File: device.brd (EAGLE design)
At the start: 38 x 50 mm, 40 parts, among them CON1 B3B-ZR, CON2 B3B-ZR, CON3 B3B-ZR, CON4 B3B-ZR, CON5 B3B-ZR, J1 S2B-PH-SM4-TB(LF)(SN), Q1 2SC2712-GR(F), Q2 2SC2712-GR(F), Q3 2SC2712-GR(F), Q4 2SC2712-GR(F)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

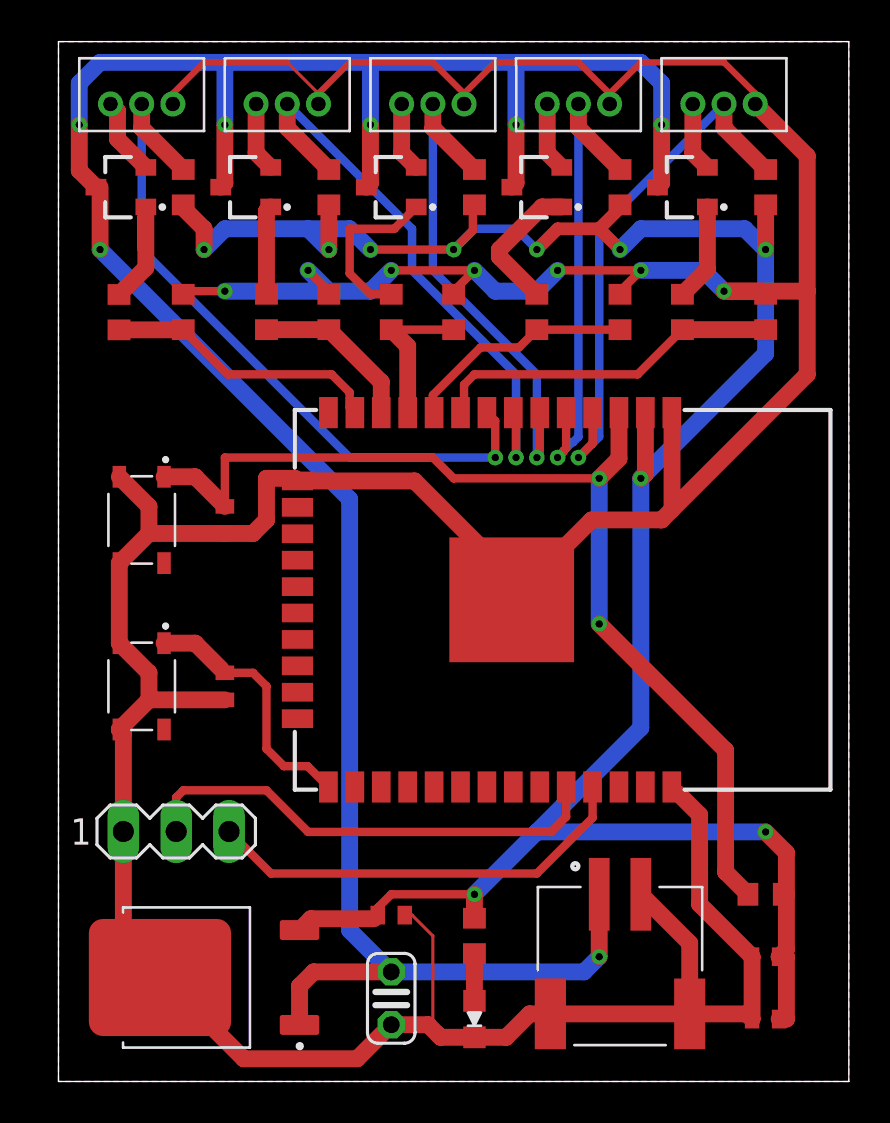
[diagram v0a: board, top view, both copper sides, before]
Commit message: Manual routing of V2.0.0
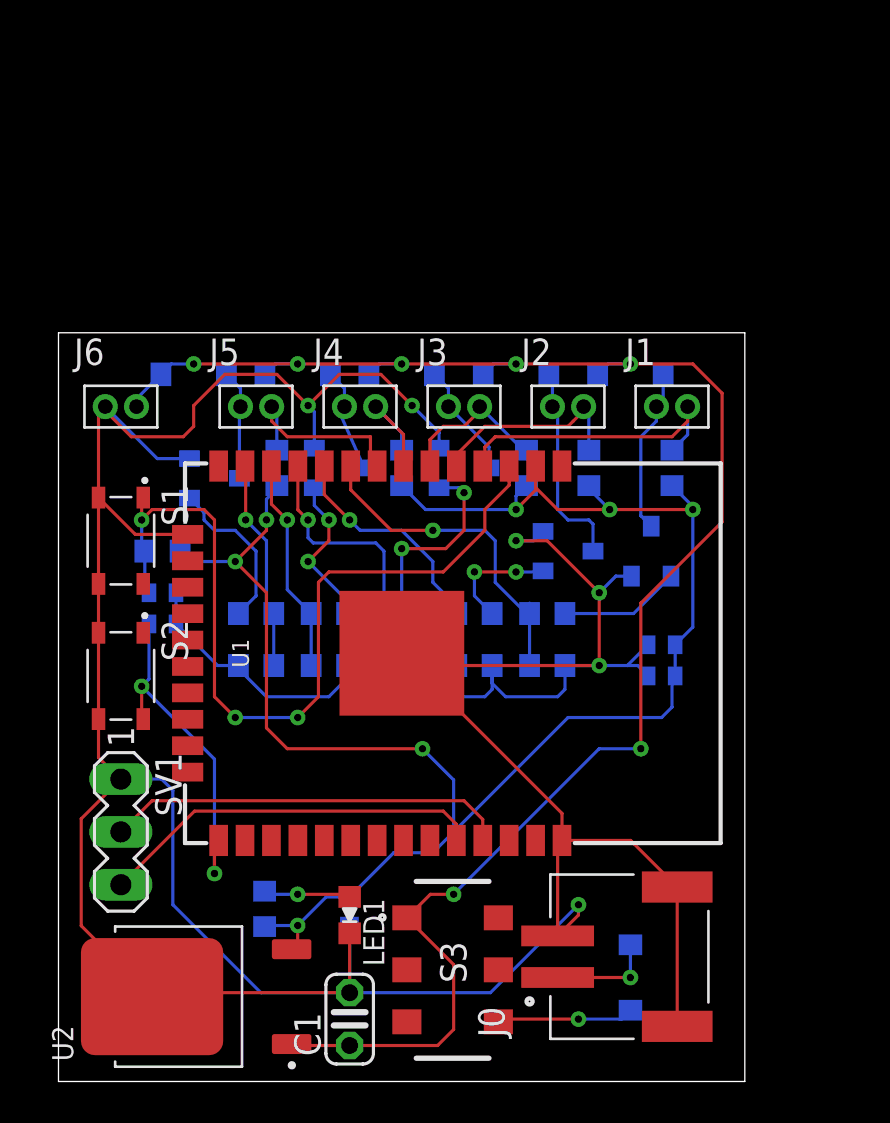
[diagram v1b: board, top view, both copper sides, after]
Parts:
- removed CON1, CON2, CON3, CON4, CON5: B3B-ZR, jst:B3B-ZR
- added D1, D2, D3, D4, D5, D6: GS1010FL, GS1010FL:SODFL3618X110N
- added J0: S2B-PH-SM4-TB(LF)(SN), S2B-PH-SM4-TB_LF__SN_:JST_S2B-PH-SM4-TB(LF)(SN)
- added J2, J3, J4, J5, J6: JST_ZH_2PIN, kanflo:JST_ZH_2PIN
- added S3: SSSS213202, SSSS213202:SSSS213202
- J1: value S2B-PH-SM4-TB(LF)(SN) -> JST_ZH_2PIN; device S2B-PH-SM4-TB_LF__SN_:JST_S2B-PH-SM4-TB(LF)(SN) -> kanflo:JST_ZH_2PIN
- moved R16 33.4 mm to (5.00, 25.5), flipped to the bottom, turned to 180 degrees
- moved J1 23.1 mm to (29.5, 32.0)
- moved R9 20.0 mm to (23.5, 20.0), flipped to the bottom, turned to 0 degrees
- moved R3 18.4 mm to (20.0, 20.0), flipped to the bottom, turned to 0 degrees
- moved Q1 17.6 mm to (28.5, 25.5), flipped to the bottom, turned to 0 degrees
- moved Q2 17.6 mm to (24.5, 25.5), flipped to the bottom
- moved R13 17.4 mm to (9.50, 20.0), flipped to the bottom, turned to 180 degrees
- moved C4 17.2 mm to (29.0, 19.5), flipped to the bottom, turned to 0 degrees
- moved R11 17.2 mm to (16.5, 20.0), flipped to the bottom, turned to 0 degrees
- moved R15 17.0 mm to (13.0, 20.0), flipped to the bottom, turned to 0 degrees
- moved R12 15.9 mm to (9.50, 22.5), flipped to the bottom, turned to 180 degrees
- moved R8 15.9 mm to (23.5, 22.5), flipped to the bottom, turned to 0 degrees
- moved C3 15.8 mm to (29.0, 21.0), flipped to the bottom, turned to 0 degrees
- moved R14 14.8 mm to (13.0, 22.5), flipped to the bottom, turned to 0 degrees
- moved R2 14.8 mm to (20.0, 22.5), flipped to the bottom, turned to 0 degrees
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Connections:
- new net N$12: D6.2, J0.1
- new net N$8: D6.1, S3.6
- net GND: now also J0.2, J0.S1, J0.S2, J6.1, Q1.2, Q2.2, Q3.2, Q4.2, Q5.2; no longer CON1.1, CON2.1, CON3.1, CON4.1, CON5.1, J1.2, J1.S1, J1.S2, U1.1
- net M1: now also D4.2, J1.1, Q1.3; no longer CON1.3, Q1.2
- net M2: now also D5.2, J2.1, Q2.3; no longer CON2.3, Q2.2
- net M3: now also D3.2, J3.1, Q3.3; no longer CON3.3, Q3.2
- net M4: now also D1.2, J4.1, Q5.3; no longer CON4.3, Q5.2
- net M5: now also D2.2, J5.1, Q4.3; no longer CON5.3, Q4.2
- net N$3: now also S2.2; no longer S2.1
- net N$4: now also SV1.2; no longer SV1.3
- net N$5: now also SV1.3; no longer SV1.2
- net S1: now also J1.2; no longer CON1.2
- net S2: now also J2.2; no longer CON2.2
- net S3: now also J3.2; no longer CON3.2
- net S4: now also J4.2; no longer CON4.2
- net S5: now also J5.2; no longer CON5.2
- net VIN: now also D1.1, D2.1, D3.1, D4.1, D5.1, J6.2, S3.1; no longer J1.1, Q1.3, Q2.3, Q3.3, Q4.3, Q5.3
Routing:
- net GND: track 248.5 -> 201.2 mm, vias 7 -> 6
- net VIN: track 124.2 -> 84.7 mm
- net 33V: track 118.9 -> 85.6 mm, vias 10 -> 7
- net S5: track 34.4 -> 9.51 mm, vias 1 -> 0
- net S4: track 27.7 -> 6.03 mm, vias 1 -> 0
- net S3: track 25.3 -> 7.56 mm, vias 1 -> 0
- net S2: track 25.2 -> 9.94 mm, vias 1 -> 0
- net S1: track 26.3 -> 14.5 mm, vias 1 -> 0
- net N$1: track 50.8 -> 41.9 mm, vias 2 -> 3
- net M2: track 3.34 -> 9.97 mm
- net N$8: track 0.00 -> 6.58 mm, vias 0 -> 1
- net MOTOR3: track 7.32 -> 13.1 mm, vias 0 -> 1
- net N$12: track 0.00 -> 5.08 mm, vias 0 -> 1
- net M1: track 3.34 -> 7.95 mm
- net N$5: track 23.1 -> 18.6 mm
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- removed copper zone on layer 1, net GND
- removed copper zone on layer 16, net GND
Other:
- board size 38 x 50 mm -> 33 x 36 mm
- board text removed: "M S G"

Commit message: Modifie board
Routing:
- net VIN: track 84.7 -> 86.8 mm
- net MOTOR3: track 13.1 -> 11.6 mm
- net N$6: track 9.95 -> 10.8 mm
- net GND: track 201.2 -> 200.4 mm
- net N$10: track 7.96 -> 7.32 mm
- net MOTOR2: track 13.4 -> 12.8 mm
- net MOTOR1: track 16.4 -> 15.8 mm
- net 33V: track 85.6 -> 86.1 mm
- added copper zone on layer 1, net GND
- added copper zone on layer 16, net GND
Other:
- board size 33 x 36 mm -> 33 x 37 mm

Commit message: update files
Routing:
- net GND: track 200.4 -> 199.2 mm
- net N$1: track 42.2 -> 41.3 mm
- net MOTOR1: track 15.8 -> 15.3 mm
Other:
- board text added: "GND"
- board text added: "M S"
- board text added: "RX"
- board text added: "TX"
